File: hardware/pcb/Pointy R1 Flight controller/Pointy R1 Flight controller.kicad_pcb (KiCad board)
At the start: 2 copper layers, 58 x 100 mm, 30 parts, among them IC1 TEENSY_4.1, J3 XT60-M, M1 Motor_Servo, M2 Motor_Servo, P1 282837-2, P2 282837-2, P3 282837-2, P4 282837-2, Q1 IRLZ44NSTRLPBF, Q2 IRLZ44NSTRLPBF, Q3 IRLZ44NSTRLPBF, U1 L7805CV, U2 GY-521, U3 MPL3115A2

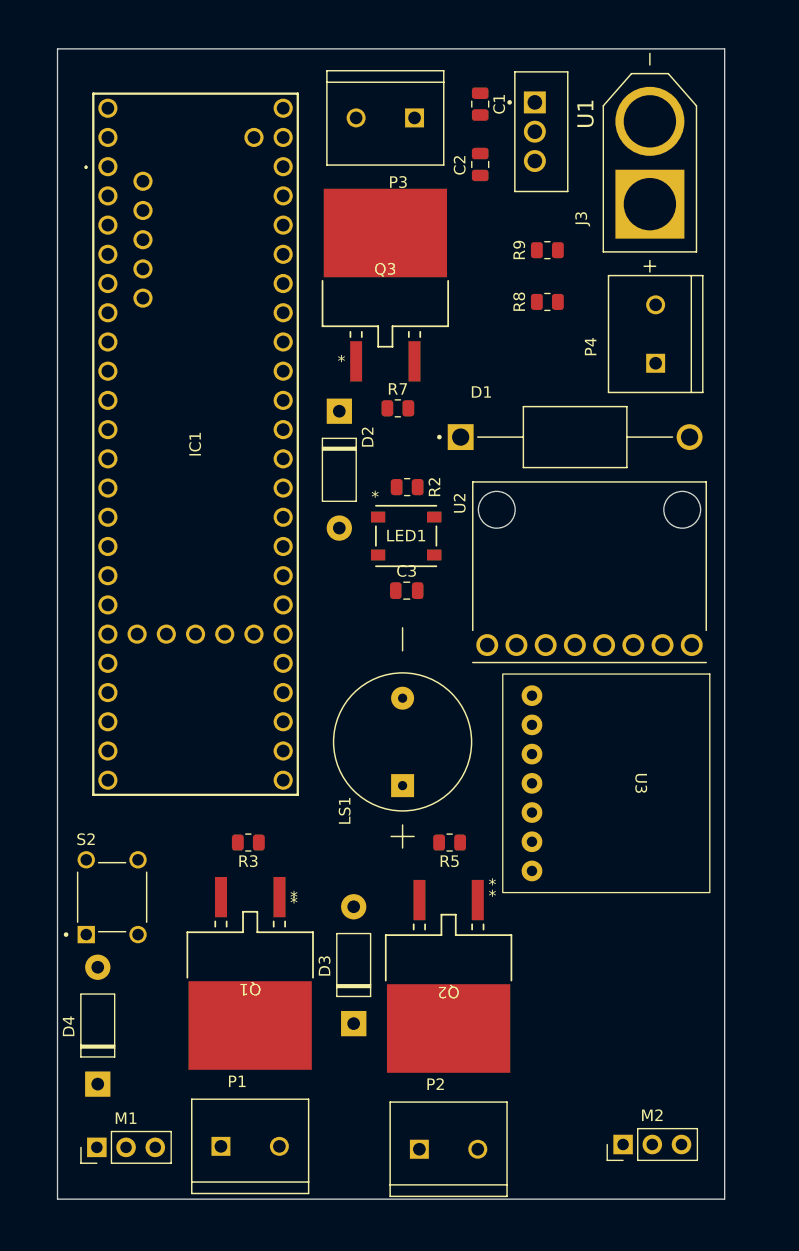
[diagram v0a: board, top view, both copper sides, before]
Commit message: Routed majority of traces for all components, excluding minor power management and gnd plane tasks
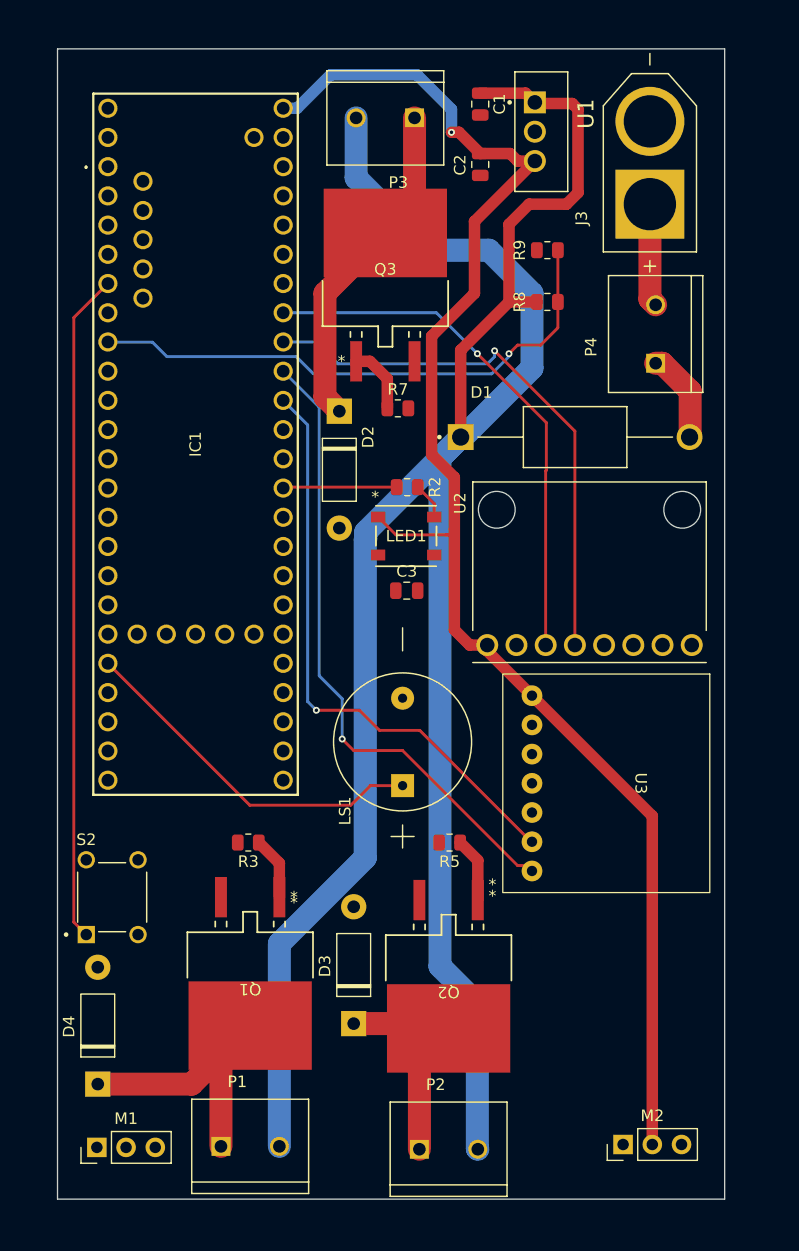
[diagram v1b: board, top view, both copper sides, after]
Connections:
- IC1 pad 13: unconnected-(IC1-SCK-Pad13) -> LED
- IC1 pad 23: BUZ -> unconnected-(IC1-A9-Pad23)
- IC1 pad 28: unconnected-(IC1-RX7-Pad28) -> BUZ
- IC1 pad 6: LED -> unconnected-(IC1-OUT1D-Pad6)
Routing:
- net 7.4V: track 0.00 -> 218.2 mm
- net +5V: track 0.00 -> 134.2 mm, vias 0 -> 1
- net SW: track 0.00 -> 58.3 mm
- net SDA1: track 0.00 -> 55.4 mm, vias 0 -> 1
- net SCL1: track 0.00 -> 51.6 mm, vias 0 -> 1
- net VOL: track 0.00 -> 48.8 mm, vias 0 -> 1
- net SDA: track 0.00 -> 48.4 mm, vias 0 -> 1
- net SCL: track 0.00 -> 46.2 mm, vias 0 -> 1
- net BUZ: track 0.00 -> 31.4 mm
- net Net-(D2-A): track 0.00 -> 29.2 mm
- net Net-(D4-A): track 0.00 -> 26.9 mm
- net Net-(D3-A): track 0.00 -> 20.0 mm
- net LED: track 0.00 -> 9.90 mm
- net BAT+: track 0.00 -> 8.96 mm
- net Net-(D1-PadA): track 0.00 -> 8.02 mm
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
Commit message: Completed routing and added gnd plane, completeting v1 of the PFC - ready for drm
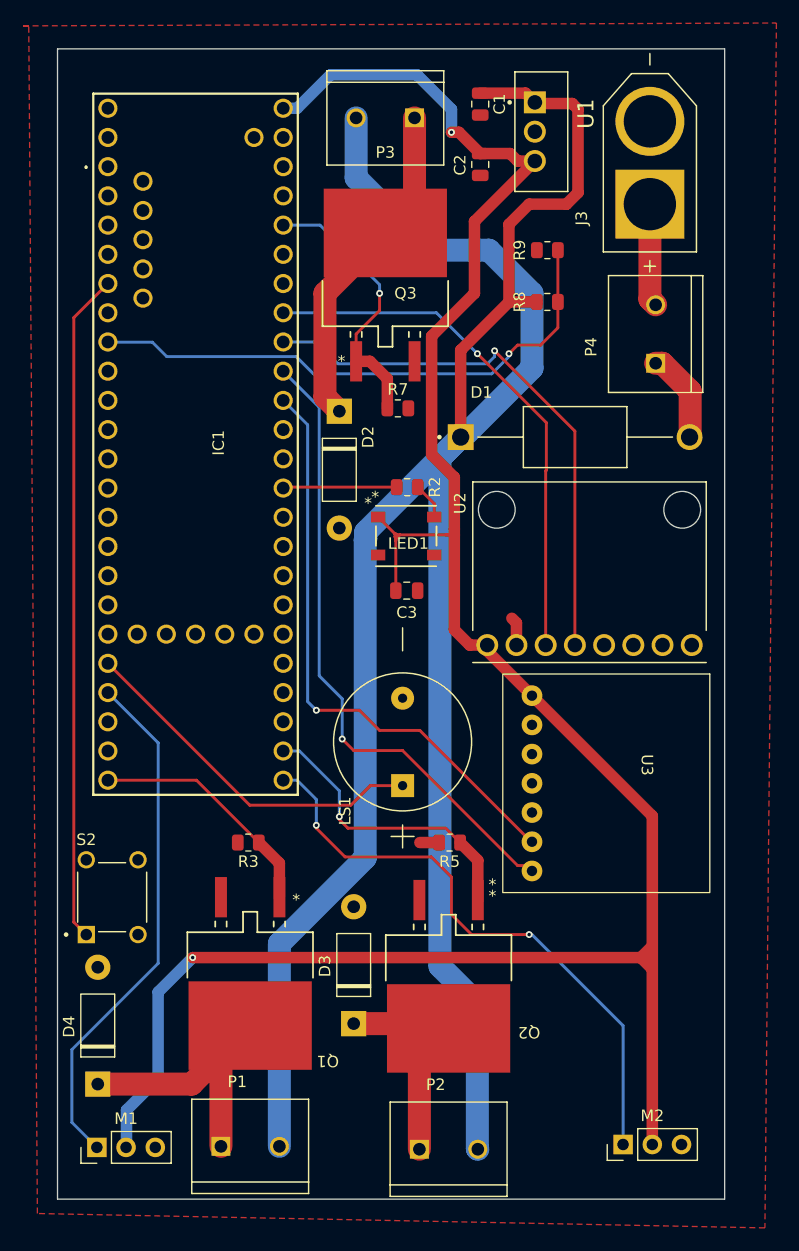
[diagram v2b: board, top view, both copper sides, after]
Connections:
- IC1 pad 14: TVC_X -> unconnected-(IC1-A0-Pad14)
- IC1 pad 15: TVC_Y -> unconnected-(IC1-A1-Pad15)
- IC1 pad 20: PY1 -> unconnected-(IC1-A6-Pad20)
- IC1 pad 21: PY2 -> unconnected-(IC1-A7-Pad21)
- IC1 pad 29: unconnected-(IC1-TX7-Pad29) -> TVC_X
- IC1 pad 32: unconnected-(IC1-OUT1B-Pad32) -> PY1
- IC1 pad 33: unconnected-(IC1-MCLK2-Pad33) -> TVC_Y
- IC1 pad 34: unconnected-(IC1-RX8-Pad34) -> PY2
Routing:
- net +5V: track 134.2 -> 200.7 mm, vias 1 -> 2
- net TVC_Y: track 0.00 -> 52.1 mm, vias 0 -> 2
- net TVC_X: track 0.00 -> 45.4 mm
- net PY2: track 5.64 -> 25.8 mm, vias 0 -> 1
- net PY3: track 5.92 -> 23.9 mm, vias 0 -> 1
- net PY1: track 5.49 -> 20.9 mm
- net GND: track 0.00 -> 4.17 mm
- added copper zone on F.Cu, net GND
